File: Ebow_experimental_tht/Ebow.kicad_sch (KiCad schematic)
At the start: 9 parts, among them J1 Conn_01x02, U1 LM386

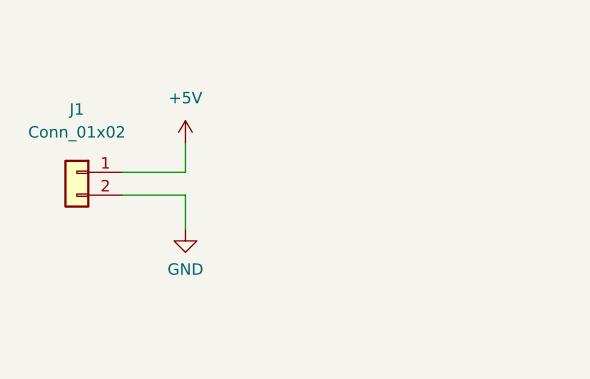
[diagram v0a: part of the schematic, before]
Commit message: updated schemas
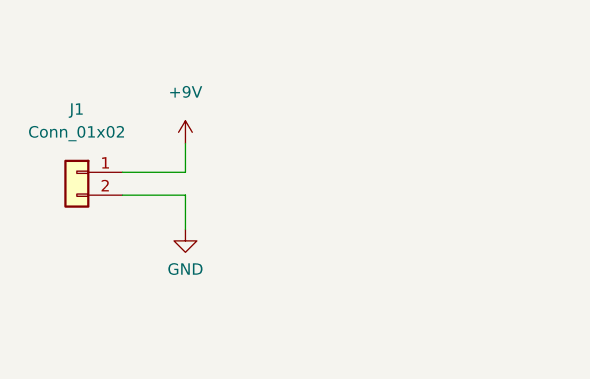
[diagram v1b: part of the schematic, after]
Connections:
- net +5V: no longer J1.1 (Pin_1)
- new net +9V: J1.1 (Pin_1)
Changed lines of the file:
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@@
+    (pin "1")
+  )
+  (symbol (lib_id "power:+9V") (at 59.055 35.56 0) (unit 1)
+    (in_bom yes) (on_board yes) (fields_autoplaced)
+    (property "Reference" "#PWR?" (id 0) (at 59.055 39.37 0)
+      (effects (font (size 1.27 1.27)) hide)
+    )
+    (property "Value" "+9V" (id 1) (at 59.055 29.845 0))
+    (property "Footprint" "" (id 2) (at 59.055 35.56 0)
+      (effects (font (size 1.27 1.27)) hide)
+    )
+    (property "Datasheet" "" (id 3) (at 59.055 35.56 0)
+      (effects (font (size 1.27 1.27)) hide)
+    )
     (pin "1")
   )
@@
     (pin "1")
   )
-  (symbol (lib_id "power:+5V") (at 59.055 35.56 0) (unit 1)
-    (in_bom yes) (on_board yes) (fields_autoplaced)
-    (property "Reference" "#PWR02" (id 0) (at 59.055 39.37 0)
-      (effects (font (size 1.27 1.27)) hide)
-    )
-    (property "Value" "+5V" (id 1) (at 59.055 30.48 0))
-    (property "Footprint" "" (id 2) (at 59.055 35.56 0)
-      (effects (font (size 1.27 1.27)) hide)
-    )
-    (property "Datasheet" "" (id 3) (at 59.055 35.56 0)
-      (effects (font (size 1.27 1.27)) hide)
-    )
-    (pin "1")
-  )
   (symbol (lib_id "Amplifier_Audio:LM386") (at 129.54 107.315 0) (unit 1)
     (in_bom yes) (on_board yes) (fields_autoplaced)
@@
       (reference "#PWR01") (unit 1) (value "GND") (footprint "")
     )
-    (path "/b14f207c-4c8e-4a7c-a74a-39cd24bc2d4c"
-      (reference "#PWR02") (unit 1) (value "+5V") (footprint "")
-    )
     (path "/92979cff-1e7c-4fc6-a0d2-82f65b7c20ae"
       (reference "#PWR03") (unit 1) (value "GND") (footprint "")
@@
       (reference "#PWR09") (unit 1) (value "GND") (footprint "")
     )
+    (path "/754f364b-6aec-4d9b-95c3-aa85053dd6ea"
+      (reference "#PWR?") (unit 1) (value "+9V") (footprint "")
+    )
     (path "/17c612b1-1712-43c4-bf42-da58958720f5"

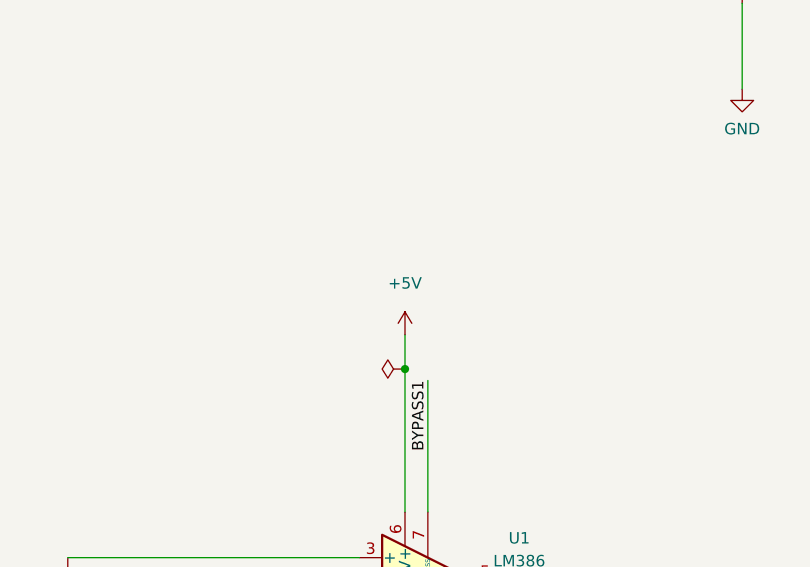
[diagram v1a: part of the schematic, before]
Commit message: updated power rail error
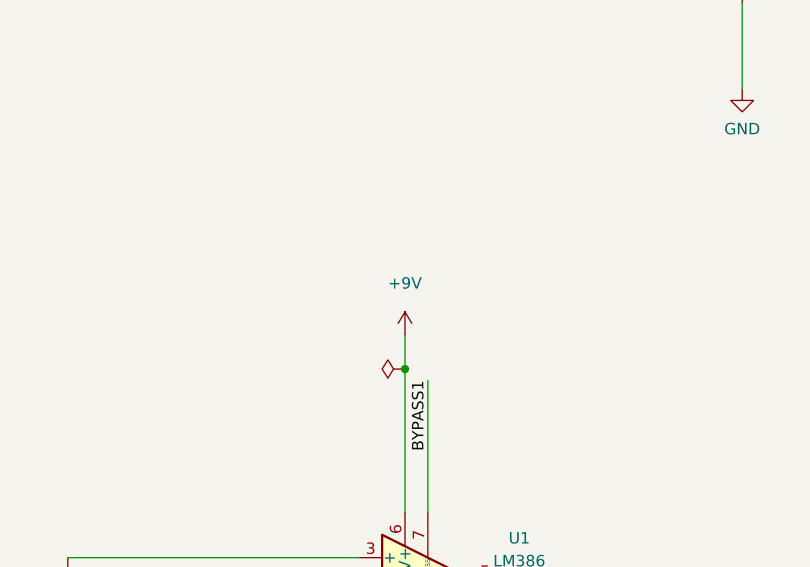
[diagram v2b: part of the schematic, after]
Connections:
- net +5V is gone; now on net +9V: U1.6 (V+)
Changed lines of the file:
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@@
-    (pin "1")
-  )
-  (symbol (lib_id "power:+5V") (at 127 80.01 0) (unit 1)
-    (in_bom yes) (on_board yes) (fields_autoplaced)
-    (property "Reference" "#PWR04" (id 0) (at 127 83.82 0)
-      (effects (font (size 1.27 1.27)) hide)
-    )
-    (property "Value" "+5V" (id 1) (at 127 74.295 0))
-    (property "Footprint" "" (id 2) (at 127 80.01 0)
-      (effects (font (size 1.27 1.27)) hide)
-    )
-    (property "Datasheet" "" (id 3) (at 127 80.01 0)
-      (effects (font (size 1.27 1.27)) hide)
-    )
     (pin "1")
   )
@@
     (pin "8")
   )
+  (symbol (lib_id "power:+9V") (at 127 80.01 0) (unit 1)
+    (in_bom yes) (on_board yes) (fields_autoplaced)
+    (property "Reference" "#PWR?" (id 0) (at 127 83.82 0)
+      (effects (font (size 1.27 1.27)) hide)
+    )
+    (property "Value" "+9V" (id 1) (at 127 74.295 0))
+    (property "Footprint" "" (id 2) (at 127 80.01 0)
+      (effects (font (size 1.27 1.27)) hide)
+    )
+    (property "Datasheet" "" (id 3) (at 127 80.01 0)
+      (effects (font (size 1.27 1.27)) hide)
+    )
+    (pin "1")
+  )
   (symbol (lib_id "power:GND") (at 118.745 147.32 0) (unit 1)
     (in_bom yes) (on_board yes) (fields_autoplaced)
@@
       (reference "#PWR03") (unit 1) (value "GND") (footprint "")
     )
-    (path "/48b7a76d-e799-461e-8984-ba9b128240cc"
-      (reference "#PWR04") (unit 1) (value "+5V") (footprint "")
-    )
     (path "/1b7db835-fd9a-4ab9-9a0d-b6f1bc70ca53"
       (reference "#PWR05") (unit 1) (value "GND") (footprint "")
@@
       (reference "#PWR?") (unit 1) (value "+9V") (footprint "")
     )
+    (path "/c07aca64-0ae8-4084-8696-3f3d253c3098"
+      (reference "#PWR?") (unit 1) (value "+9V") (footprint "")
+    )
